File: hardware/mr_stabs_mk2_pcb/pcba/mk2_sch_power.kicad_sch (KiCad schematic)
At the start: 39 parts, among them U1 INA238, U2 TPS54202DDC, U3 AP2112K-3.3

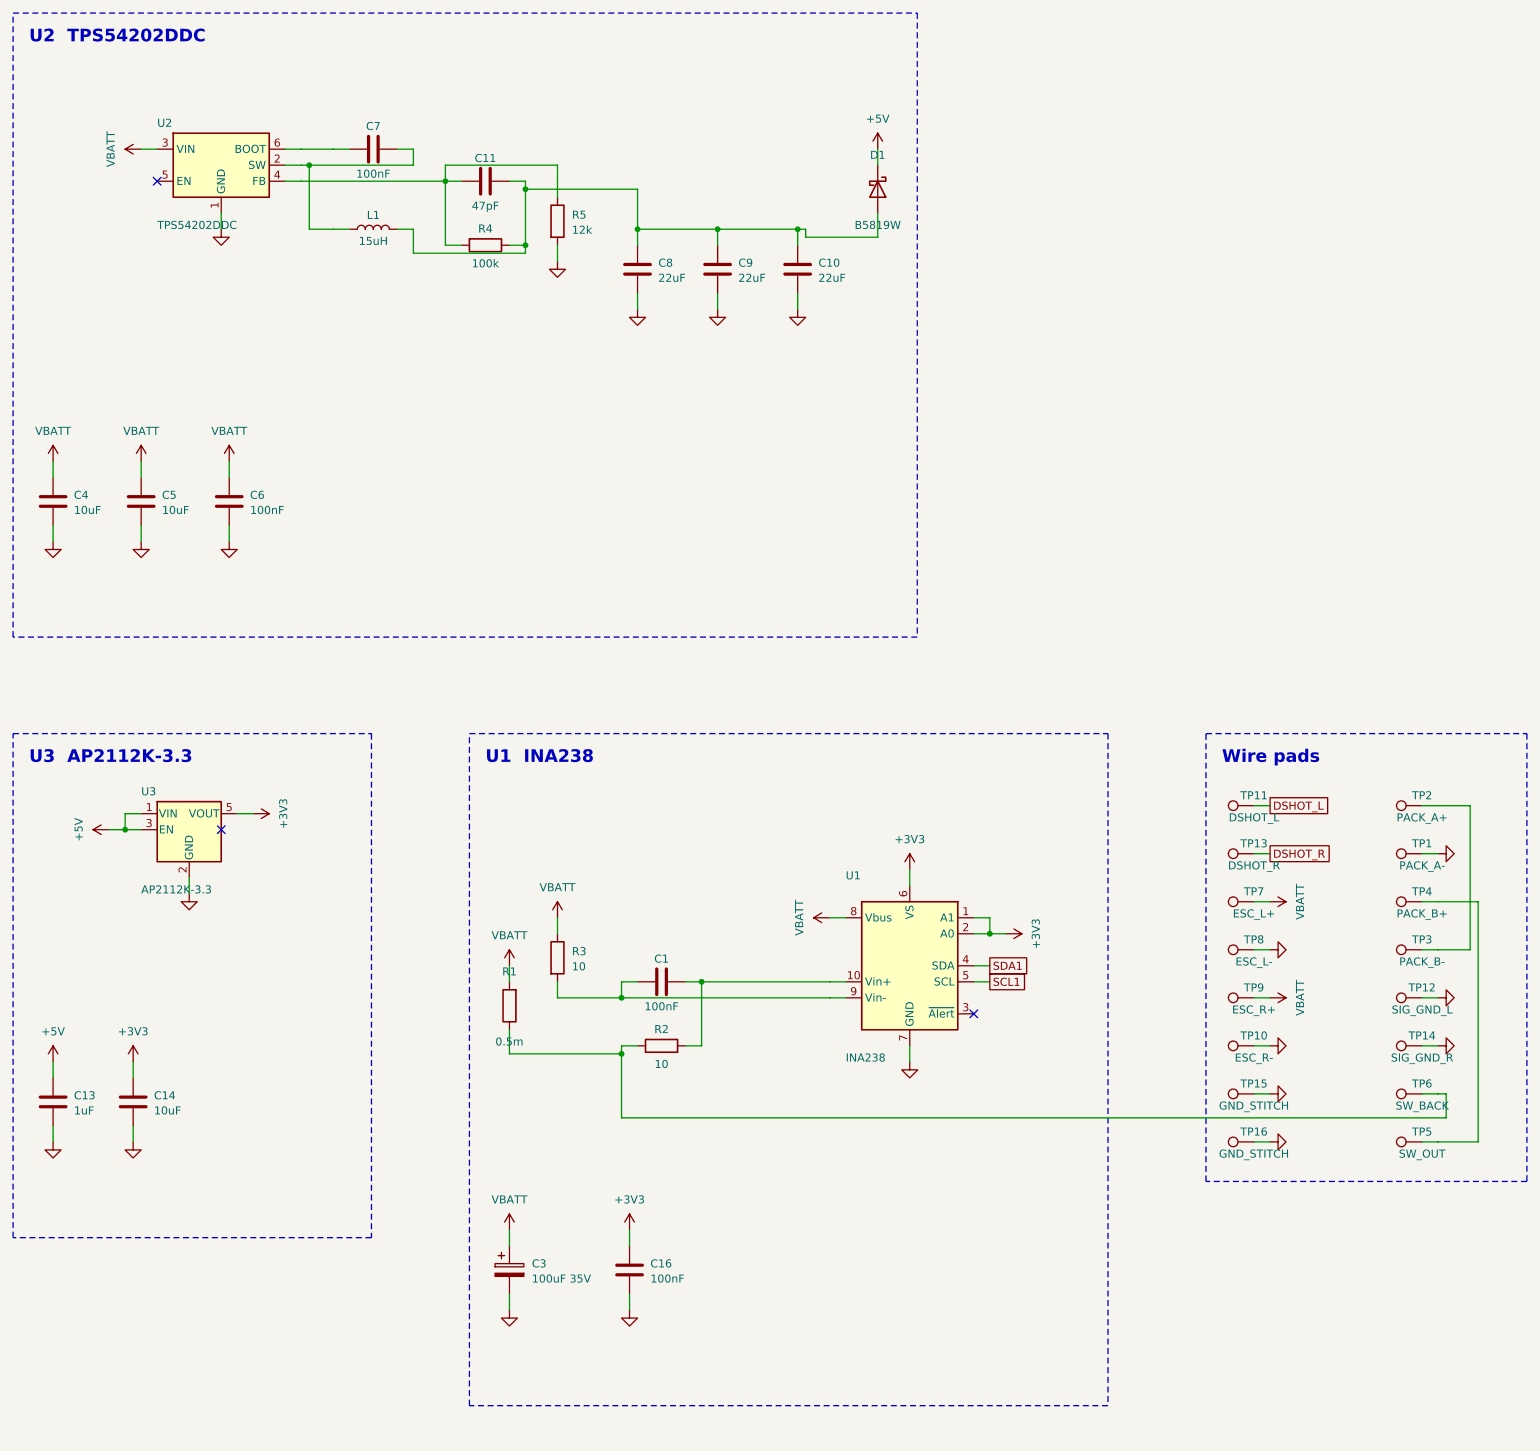
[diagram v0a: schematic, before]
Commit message: Re-route the Mk2 board at JLCPCB's 2 oz rules and fit the CPL rotations
The board orders with 2 oz outer copper, but it was routed at 0.15 mm clearance, a 1 oz
number. Against JLCPCB's 2 oz minimums (0.16 mm track, 0.20 mm space) it had 292 violations
behind a clean DRC. Re-routed at 0.20 mm: 0 errors, 0 unconnected, with mk2_routed.kicad_dru
holding the 2 oz rules so the KiCad GUI checks the same thing.

Getting the stem to route at 0.20 mm took these changes:
- Signal vias 0.5 / 0.25 mm; GND, battery and 5 V vias stay 0.6 / 0.3. Min hole 0.25 mm.
- C3 (100 uF bulk) back on the right ear beside the shunt. Its feed across the stem never
  routed at 2 oz spacing, and a prewired track there walled off the signals. It gives up the
  stem's protection from a dislodged motor.
- INA238 VBUS on BAT_IN, the F pour under the pin. Reads the shunt drop high, at most 35 mV at
  a 70 A stall; current sensing is unchanged.
- B keepouts hold the VBATT pour's neck (shunt to ESC_L+) and R3's Kelvin tap open: signal
  tracks had split the pour and left the ESC current on a track.
- F VBATT patch over the buck input, with the B VBATT pour extended under it so every piece
  stitches down. C6 turned to face it; INA238 moved 0.3 mm off the rear edge.

The copper IR solve now gives a 23.8 mV VBATT drop at 70 A, down from 42.4 mV.

cpl.csv angles and centres are fitted to JLCPCB's own footprint for each LCSC number
(cpl_check.csv). KiCad's angles would have placed C3 reversed and five ICs 90 degrees out.
R5 and U5 no longer have vias in their pads; C14 and C10 still do (open question 8).

Co-Authored-By: Claude Opus 5.5 <noreply@anthropic.com>
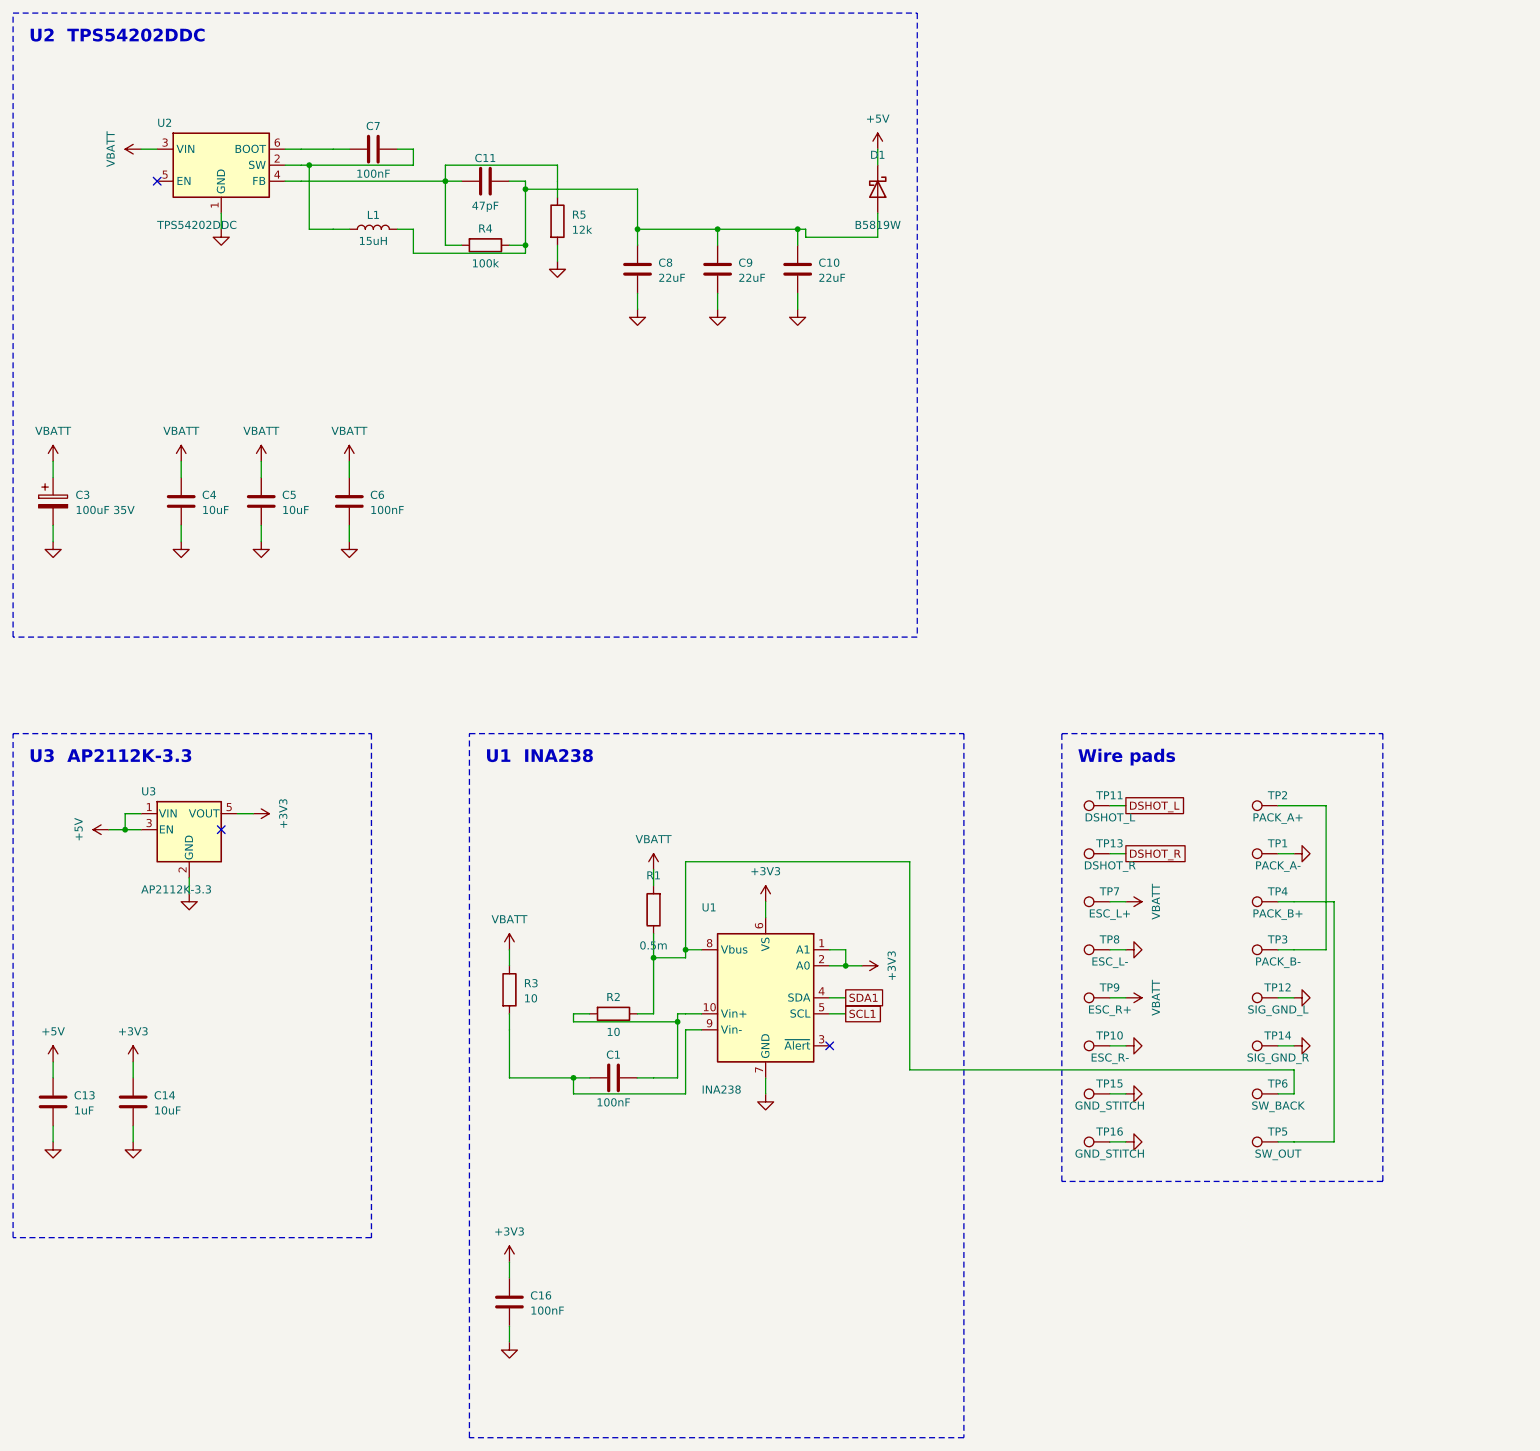
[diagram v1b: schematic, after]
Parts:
- removed C16, C7: 100nF, symbol Device:C
- removed L1: 15uH, symbol Device:L
- added R4: 100k, symbol Device:R
- added R5: 12k, symbol Device:R
- added TP11: DSHOT_L, symbol Connector:TestPoint
- C16: renamed from TP11; value DSHOT_L -> 100nF; symbol Connector:TestPoint -> Device:C
- C7: renamed from R4; value 100k -> 100nF; symbol Device:R -> Device:C
- L1: renamed from R5; value 12k -> 15uH; symbol Device:R -> Device:L
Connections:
- net +3V3: now also C16.1
- net DSHOT_L: now also TP11.1; no longer C16.1
- net GND: now also C16.2, R5.2; no longer L1.2
- net VBATT: no longer U1.8 (Vbus)
- net at C10.1, C11.1, C8.1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: now also L1.2, R4.1; no longer C7.1
- net at C7.2, L1.1: now also U2.2 (SW); no longer C11.2, U2.4 (FB)
- net at R1.1, R2.1, TP6.1: now also U1.8 (Vbus)
- net at U2.6 (BOOT): now also C7.1
- new net: C11.2, R4.2, R5.1, U2.4 (FB)
